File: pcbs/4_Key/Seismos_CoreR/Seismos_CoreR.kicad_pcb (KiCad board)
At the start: 2 copper layers, 147 x 78 mm, 27 parts, among them J1 SM09B-SRSS-TB(LF)(SN), J2 SM09B-SRSS-TB(LF)(SN), J3 SM09B-SRSS-TB(LF)(SN), J4 SM09B-SRSS-TB(LF)(SN), J5 SM09B-SRSS-TB(LF)(SN), J6 SM09B-SRSS-TB(LF)(SN), J7 Conn_01x05_Pin, J8 MJ-4PP-9-Lily58, J9 SM09B-SRSS-TB(LF)(SN), SW1 RotaryEncoder_Switch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

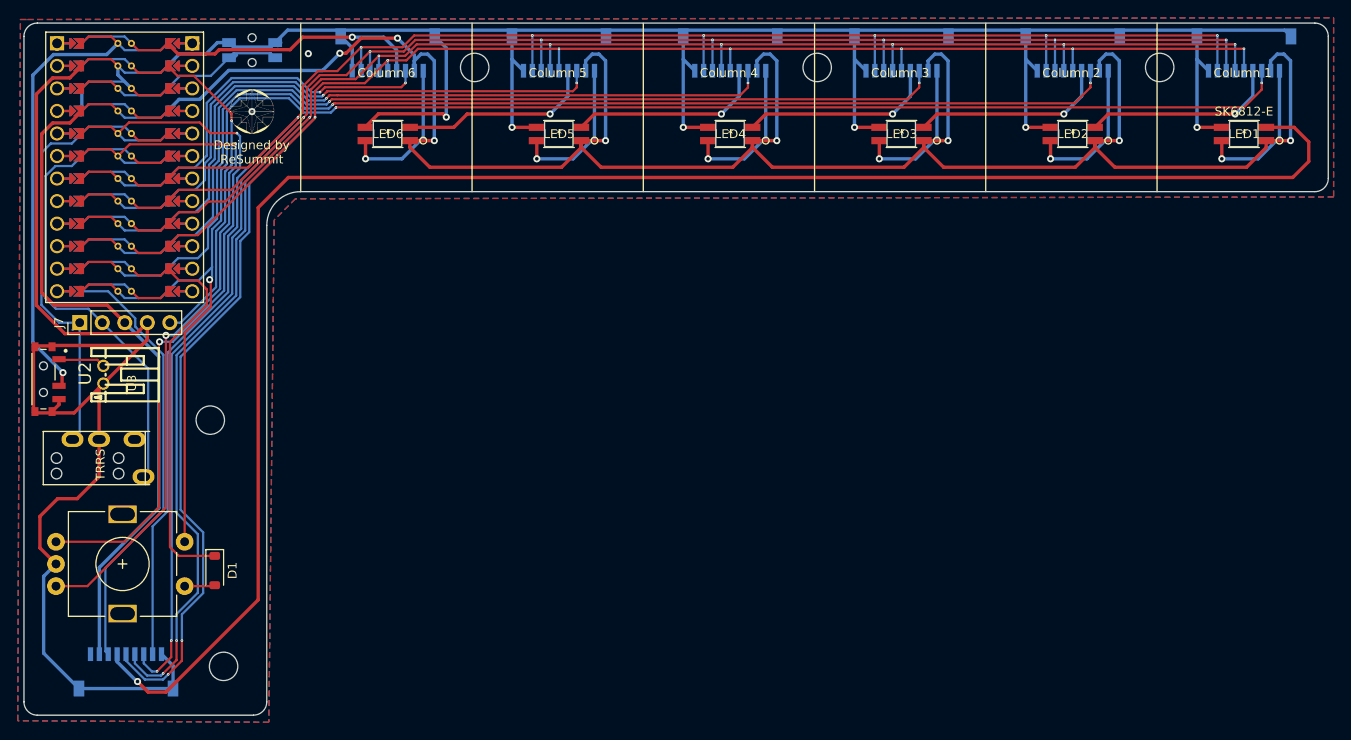
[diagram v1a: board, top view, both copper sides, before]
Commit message: Replaced microvias with very small vias
Also added small JLCJLCJLCJLC text for JLCPCB.

JLCPCB doesn't allow for blind microvias... so annoyingly I had to
reroute the row and column wiring. Luckily the 4 key doesn't use
microvias so that one is okay.
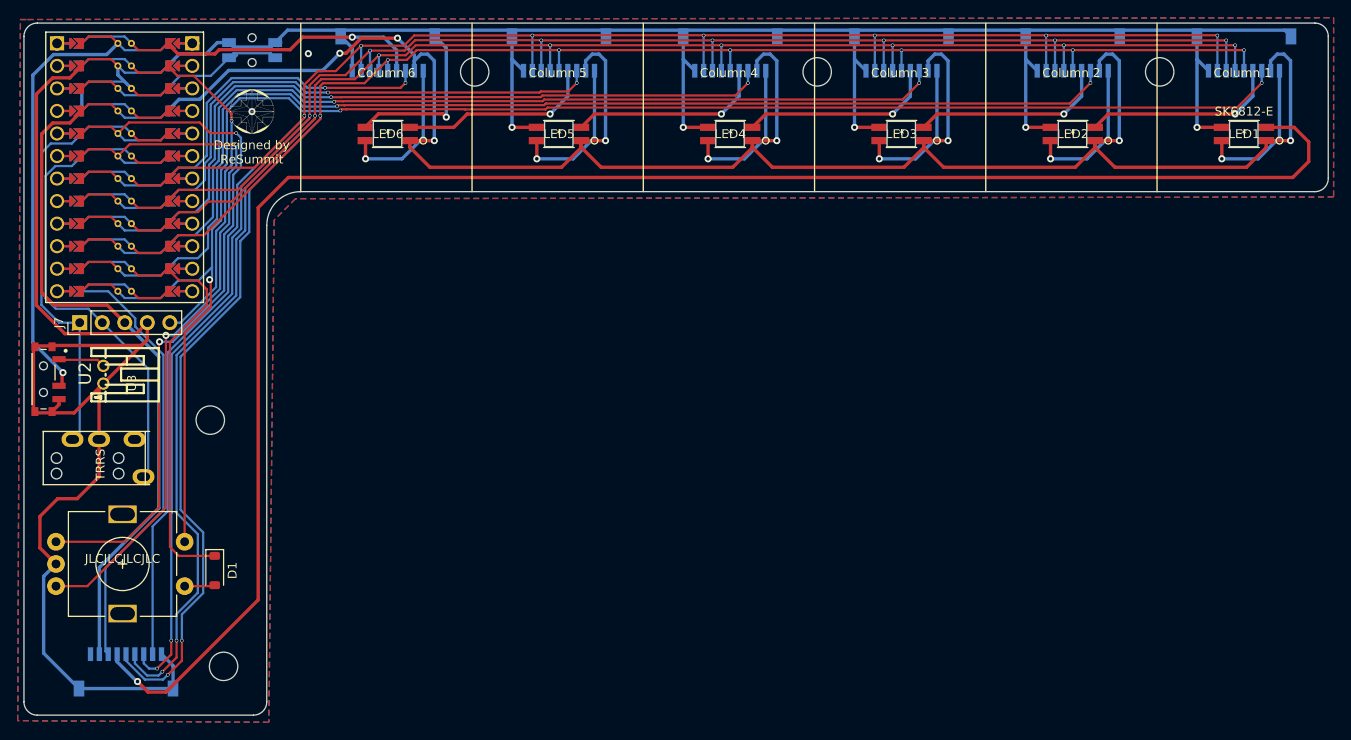
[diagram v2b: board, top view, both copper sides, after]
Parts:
- moved ? 0.50 mm to (80.8, 25.5)
- moved ? 0.50 mm to (158.0, 25.5)
- moved ? 0.50 mm to (119.4, 25.5)
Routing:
- net /Row1: track 216.6 -> 217.6 mm
- net /Col_In2: track 59.2 -> 58.6 mm
- net /Col_In3: track 80.7 -> 80.1 mm
- net /Col_In6: track 177.8 -> 177.3 mm
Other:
- board text added: "JLCJLCJLCJLC"

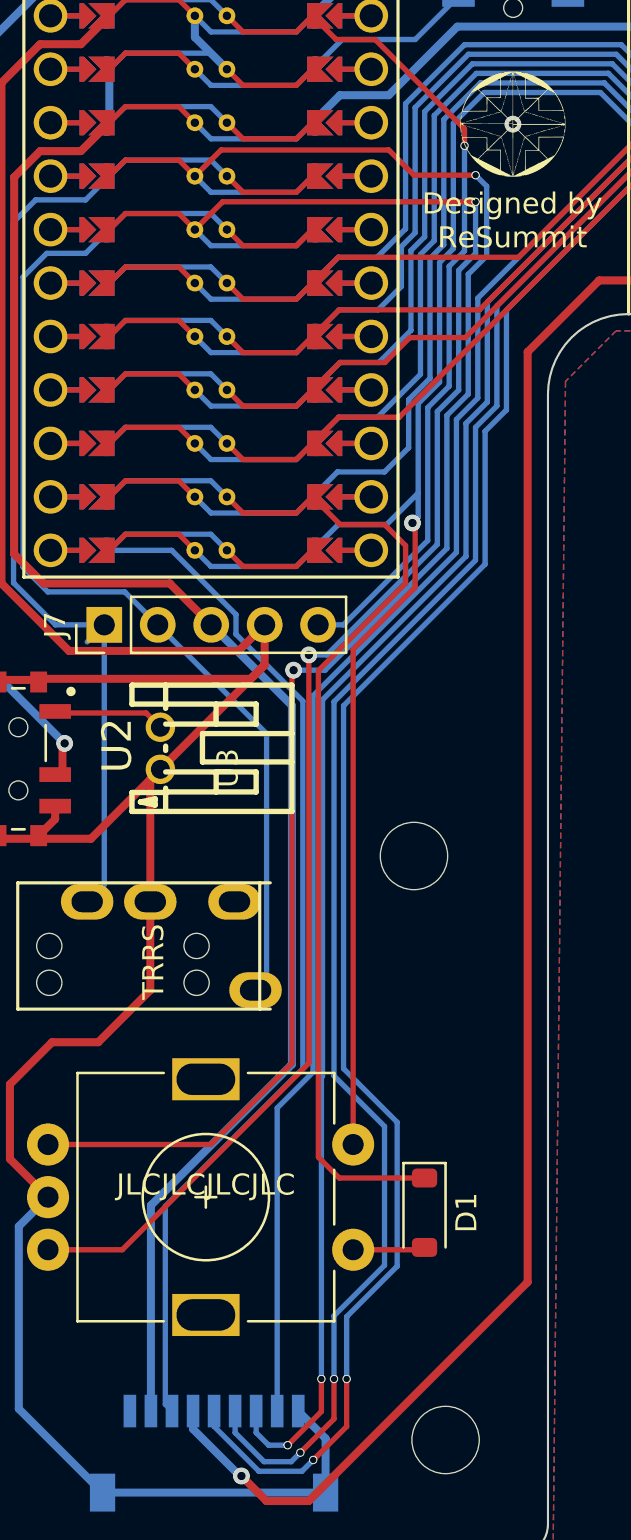
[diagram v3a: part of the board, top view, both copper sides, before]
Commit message: Last look over CoreL and removed microvias
CoreR has been verified by JLCPCB and is good to go. I forgot to add
teardrops to it so it is now added. CoreL on the other hand had some
more microvias near the JST SH conectors and under the rotary
encoder. These have been removed.

NOTE: Due to the microvia conversion, the previous commit was when the
NTPH holes near the columns have been shifted down by 0.5 mm. This will
be reflected in the case shortly but not yet as of now.

We'll see what JLCPCB says but it looks okay; hopefully I will get
results in a week or so.
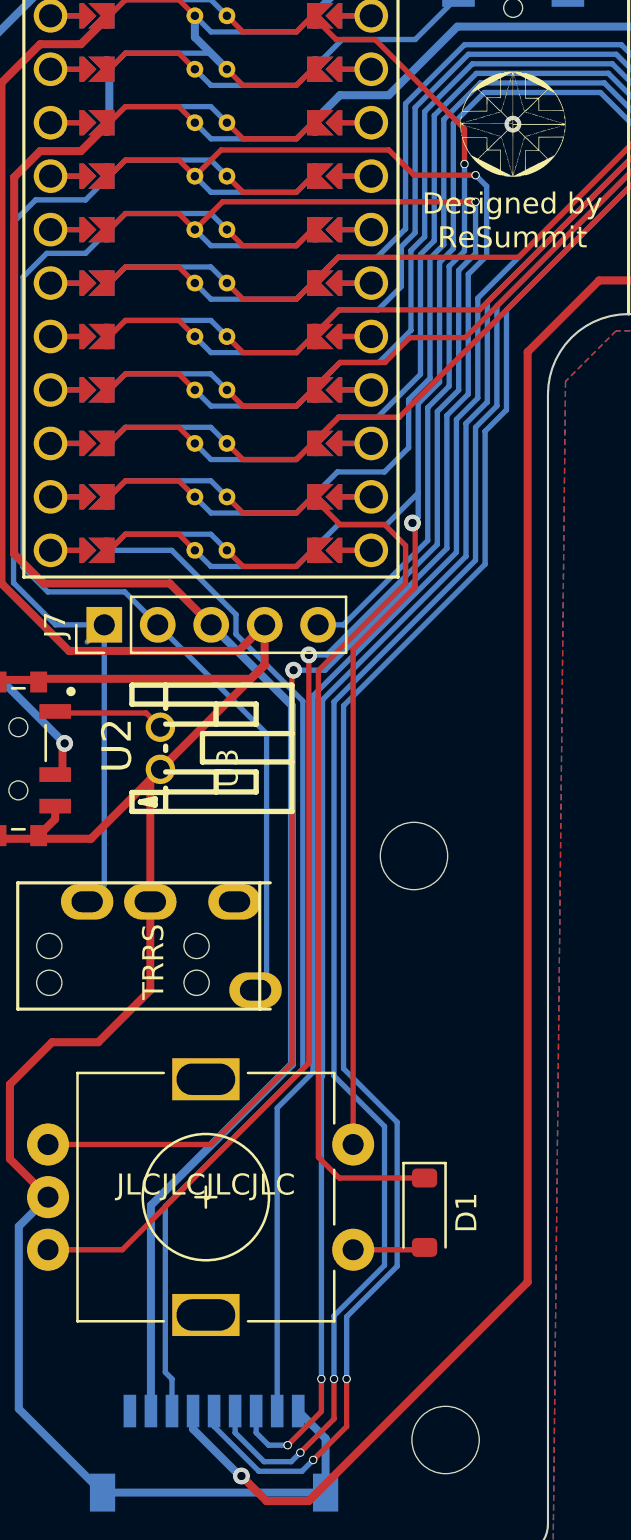
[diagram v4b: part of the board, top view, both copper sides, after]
